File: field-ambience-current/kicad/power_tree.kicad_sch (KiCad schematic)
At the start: 12 parts, among them J1 USB_C_Receptacle (TYPE-C-31-M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, U5 AP7361A-33 1A LDO (+5V->+3V3,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

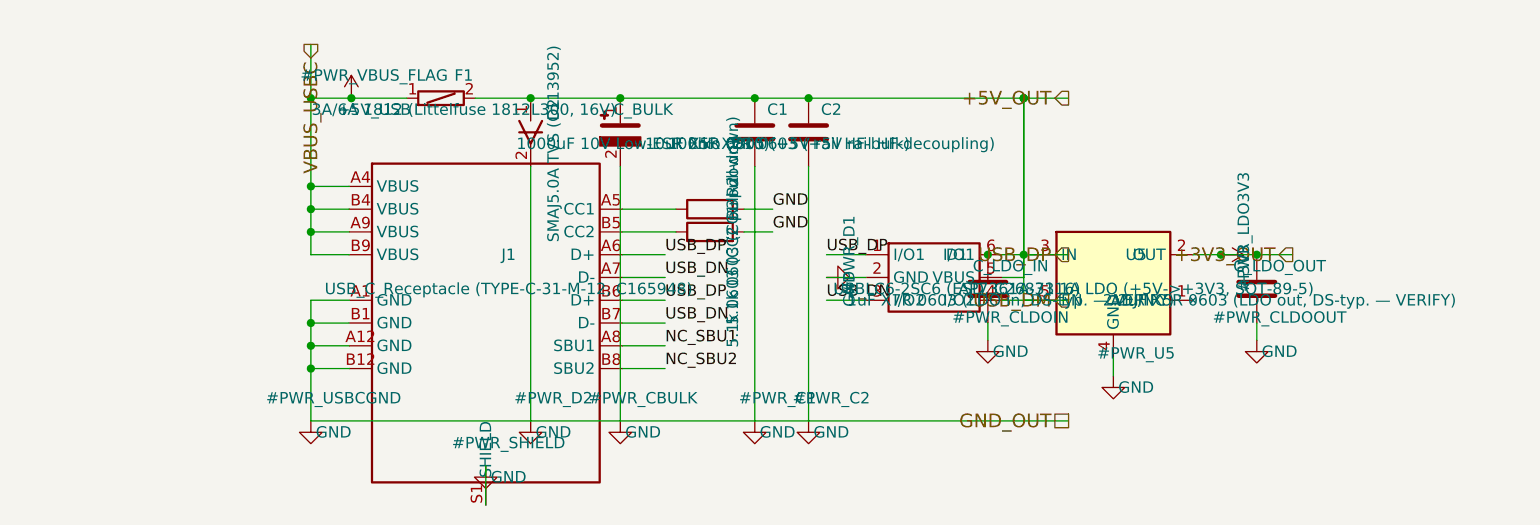
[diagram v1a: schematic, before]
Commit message: pcb(r18.6): Engineering-Verifikation — AP7361C-Pinout-Fix, TPS61089-Quelle, Custom-FP, BOM-LCSC, ADR-MIDI
Reaktion auf User-Korrekturen aus öffentlichen Datasheets. Vier
🔴-Blocker geschlossen, einer auf eine Design-Entscheidung umklassifiziert.

=== AP7361A-Pinout war FALSCH — gefixt + AP7361C ===

r18.5-Annahme: 1=ADJ/NC, 2=OUT, 3=IN, 4=GND, 5=EN.
Korrekt (Diodes-DS via mouser.de/datasheet/3/175/1/AP7361.pdf,
User-verifiziert):
    1=EN, 2=GND, 3=ADJ/NC, 4=IN, 5=OUT

Hätte zu einem totem Board geführt (IN/OUT/EN vertauscht).

Zusätzlich:
- Symbol auf AP7361C umbenannt (Diodes markiert AP7361 als NRND ->
  use AP7361C; gleicher SOT-89-5-Pinout)
- AP7361C-33Y5-13 = LCSC C460397 (SOT-89-5) statt r18.5-Kandidat
  C150719 (= SOT-223, falsches Package; verworfen)
- Cin/Cout 4.7 µF X5R 0603 (DS-Empfehlung, statt 1µF/2.2µF)
- Symbol-Pinmap + power_tree-Verdrahtung umgebaut: EN-Pin liegt
  jetzt links oben (statt links unten), IN links unten, OUT
  rechts oben — neu gerechnete Stub-Wires + Junctions

=== TPS61089-Footprint + Datenblatt-Anchor ===

- Symbol-Pinmap (1=FSW … 11=SW) verifiziert gegen TI Rev C Tabelle 6-1
  (User-Quelle ti.com/lit/gpn/tps61089) — als PIN_SOURCE-Property
- Footprint-Name auf RNR0011A-Konvention 2.0x2.5mm VQFN-HR
- RNSR-PDF → datasheets/legacy/TPS61089RNSR_wrong_variant.pdf

=== Encoder C209762 (NRND, Prototype-OK) ===

- MPN EC11J1525402, LCSC C209762 (JLCPCB-verifiziert)
- Datasheet-Link auf JLCPCB-Detail-Seite (ALPS-Drawing nicht öffentlich)
- Status: NRND als Property — Prototype-OK, Serie braucht Ersatztyp
- FP_VERIFY-Hinweis (EC11J ist SMD, der KiCad-Standard-FP EC11E ist THT)

=== Custom-Footprint für HX 12x12 (SW6-10) ===

- libraries/field_ambience.pretty/SW_HX_12x12x7.3_SMD-4P.kicad_mod
  basierend auf LCSC-Daten von C36498966:
  - SMD-4P, 11.8x11.8mm Body, 7.3mm Höhe
  - 4 Pads je 2.5x1.5mm auf 7mm-Pitch (X+Y)
  - SPST: gegenüberliegende Pads verbunden (1↔1, 2↔2)
  - Silkscreen + Pin-1-Dot + Courtyard +0.25mm IPC-7351B
- fp-lib-table um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
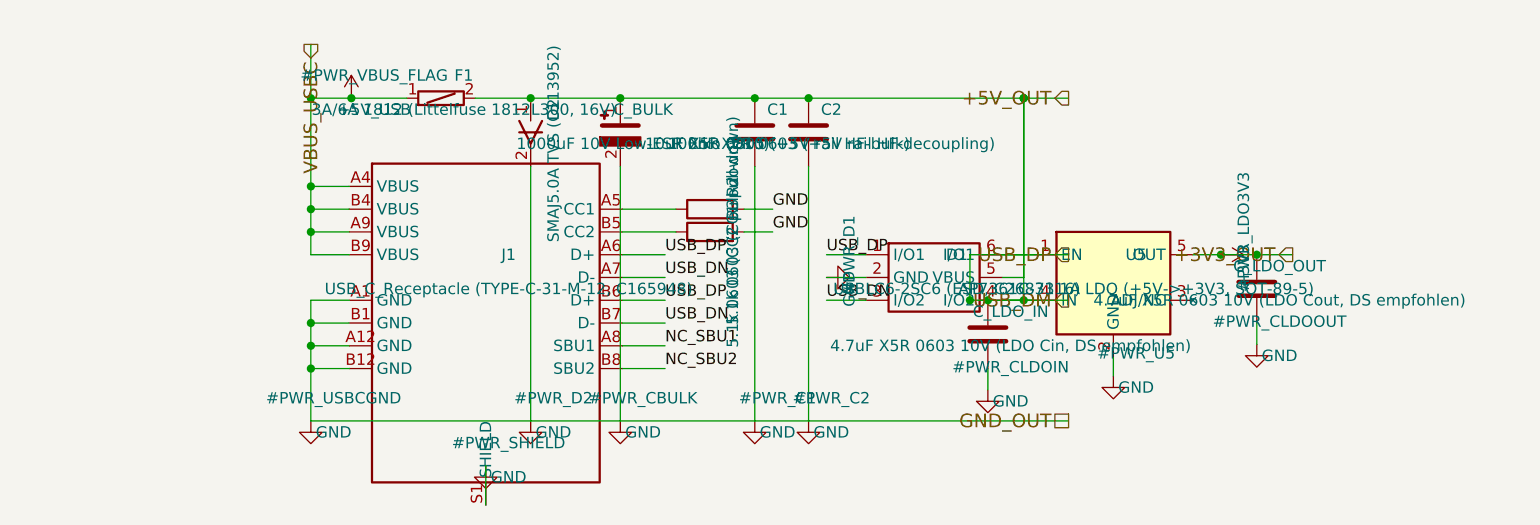
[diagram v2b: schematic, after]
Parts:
- C_LDO_IN: value 1uF X7R 0603 (LDO in, DS-typ. — VERIFY) -> 4.7uF X5R 0603 10V (LDO Cin, DS empfohlen); LCSC C15849 -> C46653; MPN CL10A105KB8NNNC -> GRM188R61A475KE15D
- C_LDO_OUT: value 2.2uF X5R 0603 (LDO out, DS-typ. — VERIFY) -> 4.7uF X5R 0603 10V (LDO Cout, DS empfohlen); LCSC TBD-VERIFY -> C46653; MPN TBD-VERIFY (2.2uF/10V X5R 0603) -> GRM188R61A475KE15D
- U5: value AP7361A-33 1A LDO (+5V->+3V3, SOT-89-5) -> AP7361C-33 1A LDO (+5V->+3V3, SOT-89-5); symbol Regulator_Linear:AP7361A -> Regulator_Linear:AP7361C; FP_VERIFY SOT-89-5-Footprint-Name + Land-Pattern in Phase-3-GUI pruef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 -> SOT-89-5-Land-Pattern (Tab-Hoehe + Pin-Pitch 1.5mm) in Phas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; LCSC TBD-VERIFY (C156144 in SPEC war FALSCH = 910R-Widerstand; K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 -> C460397; MPN AP7361A-33ER-13 -> AP7361C-33Y5-13; NOTE (none) -> AP7361 ist NRND; AP7361C ist der Nachfolger (gleicher Pinou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; PIN_SOURCE (none) -> Diodes-DS via mouser.de/datasheet/3/175/1/AP7361.pdf (User-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; PIN_VERIFY B-LDO: SOT-89-5-Pinout (1=ADJ/NC,2=OUT,3=IN,4=GND,5=EN) geg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 -> (none); Package (none) -> SOT-89-5 (NICHT SOT-223)
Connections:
- net +3V3: now also U5.5 (OUT); no longer U5.2 (OUT)
- net +5V_OUT: now also C_LDO_IN.1, U5.1 (EN), U5.4 (IN); no longer U5.3 (IN), U5.5 (EN)
- net GND: now also U5.2 (GND); no longer U5.4 (GND)
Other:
- moved on the sheet: C_LDO_IN
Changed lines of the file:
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@@
       (project "field_ambience"
         (path "/8f124281-8f89-47ab-aa39-bcbf8f1e5e4d" (reference "#PWR_SHIELD") (unit 1)))))
-  (symbol (lib_id "Regulator_Linear:AP7361A") (at 120.0 80.0 0) (unit 1)
+  (symbol (lib_id "Regulator_Linear:AP7361C") (at 120.0 80.0 0) (unit 1)
     (in_bom yes) (on_board yes) (dnp no)
       (property "Reference" "U5" (at 122.54 77.46 0)
         (effects (font (size 1.27 1.27))))
-      (property "Value" "AP7361A-33 1A LDO (+5V->+3V3, SOT-89-5)" (at 122.54 81.27 0)
+      (property "Value" "AP7361C-33 1A LDO (+5V->+3V3, SOT-89-5)" (at 122.54 81.27 0)
         (effects (font (size 1.27 1.27))))
       (property "Footprint" "Package_TO_SOT_SMD:SOT-89-5" (at 120.0 80.0 0)
         (effects (font (size 1.27 1.27)) hide))
-      (property "Datasheet" "https://www.diodes.com/assets/Datasheets/AP7361.pdf" (at 120.0 80.0 0)
-        (effects (font (size 1.27 1.27)) hide))
-      (property "MPN" "AP7361A-33ER-13" (at 122.54 83.81 0)
-        (effects (font (size 1.27 1.27)) hide))
-      (property "LCSC" "TBD-VERIFY (C156144 in SPEC war FALSCH = 910R-Widerstand; Kandidat C150719 = AP7361-33E-13)" (at 122.54 85.08 0)
-        (effects (font (size 1.27 1.27)) hide))
-      (property "PIN_VERIFY" "B-LDO: SOT-89-5-Pinout (1=ADJ/NC,2=OUT,3=IN,4=GND,5=EN) gegen offizielles AP7361A-DS pruefen — IN/OUT-Tausch = totes Board" (at 122.54 86.35 0)
-        (effects (font (size 1.27 1.27)) hide))
-      (property "FP_VERIFY" "SOT-89-5-Footprint-Name + Land-Pattern in Phase-3-GUI pruefen" (at 122.54 87.62 0)
+      (property "Datasheet" "https://www.mouser.de/datasheet/3/175/1/AP7361.pdf" (at 120.0 80.0 0)
+        (effects (font (size 1.27 1.27)) hide))
+      (property "MPN" "AP7361C-33Y5-13" (at 122.54 83.81 0)
+        (effects (font (size 1.27 1.27)) hide))
+      (property "LCSC" "C460397" (at 122.54 85.08 0)
+        (effects (font (size 1.27 1.27)) hide))
+      (property "Package" "SOT-89-5 (NICHT SOT-223)" (at 122.54 86.35 0)
+        (effects (font (size 1.27 1.27)) hide))
+      (property "PIN_SOURCE" "Diodes-DS via mouser.de/datasheet/3/175/1/AP7361.pdf (User-verifiziert): 1=EN,2=GND,3=ADJ/NC,4=IN,5=OUT" (at 122.54 87.62 0)
+        (effects (font (size 1.27 1.27)) hide))
+      (property "NOTE" "AP7361 ist NRND; AP7361C ist der Nachfolger (gleicher Pinout am SOT-89-5)" (at 122.54 88.89 0)
+        (effects (font (size 1.27 1.27)) hide))
+      (property "FP_VERIFY" "SOT-89-5-Land-Pattern (Tab-Hoehe + Pin-Pitch 1.5mm) in Phase-3-GUI gegen Diodes-DS Page Mechanical Outline pruefen" (at 122.54 90.16 0)
         (effects (font (size 1.27 1.27)) hide))
     (instances
@@
       (project "field_ambience"
         (path "/8f124281-8f89-47ab-aa39-bcbf8f1e5e4d" (reference "#PWR_U5") (unit 1)))))
-  (symbol (lib_id "Device:C") (at 106 81.27 0) (unit 1)
-    (in_bom yes) (on_board yes) (dnp no)
-      (property "Reference" "C_LDO_IN" (at 108.54 78.72999999999999 0)
-        (effects (font (size 1.27 1.27))))
-      (property "Value" "1uF X7R 0603 (LDO in, DS-typ. — VERIFY)" (at 108.54 82.53999999999999 0)
-        (effects (font (size 1.27 1.27))))
-      (property "Footprint" "Capacitor_SMD:C_0603_1608Metric" (at 106 81.27 0)
-        (effects (font (size 1.27 1.27)) hide))
-      (property "Datasheet" "~" (at 106 81.27 0)
-        (effects (font (size 1.27 1.27)) hide))
-      (property "MPN" "CL10A105KB8NNNC" (at 108.54 85.08 0)
-        (effects (font (size 1.27 1.27)) hide))
-      (property "LCSC" "C15849" (at 108.54 86.35 0)
+  (symbol (lib_id "Device:C") (at 106 86.35000000000001 0) (unit 1)
+    (in_bom yes) (on_board yes) (dnp no)
+      (property "Reference" "C_LDO_IN" (at 108.54 83.81 0)
+        (effects (font (size 1.27 1.27))))
+      (property "Value" "4.7uF X5R 0603 10V (LDO Cin, DS empfohlen)" (at 108.54 87.62 0)
+        (effects (font (size 1.27 1.27))))
+      (property "Footprint" "Capacitor_SMD:C_0603_1608Metric" (at 106 86.35000000000001 0)
+        (effects (font (size 1.27 1.27)) hide))
+      (property "Datasheet" "~" (at 106 86.35000000000001 0)
+        (effects (font (size 1.27 1.27)) hide))
+      (property "MPN" "GRM188R61A475KE15D" (at 108.54 90.16000000000001 0)
+        (effects (font (size 1.27 1.27)) hide))
+      (property "LCSC" "C46653" (at 108.54 91.43 0)
         (effects (font (size 1.27 1.27)) hide))
     (instances
       (project "field_ambience"
         (path "/8f124281-8f89-47ab-aa39-bcbf8f1e5e4d" (reference "C_LDO_IN") (unit 1)))))
-  (symbol (lib_id "Power:GND") (at 106 87.0 0) (unit 1)
-    (in_bom yes) (on_board yes) (dnp no)
-      (property "Reference" "#PWR_CLDOIN" (at 108.54 84.46 0)
-        (effects (font (size 1.27 1.27))))
-      (property "Value" "GND" (at 108.54 88.27 0)
-        (effects (font (size 1.27 1.27))))
-      (property "Footprint" "" (at 106 87.0 0)
-        (effects (font (size 1.27 1.27)) hide))
-      (property "Datasheet" "~" (at 106 87.0 0)
+  (symbol (lib_id "Power:GND") (at 106 92.54 0) (unit 1)
+    (in_bom yes) (on_board yes) (dnp no)
+      (property "Reference" "#PWR_CLDOIN" (at 108.54 90.0 0)
+        (effects (font (size 1.27 1.27))))
+      (property "Value" "GND" (at 108.54 93.81 0)
+        (effects (font (size 1.27 1.27))))
+      (property "Footprint" "" (at 106 92.54 0)
+        (effects (font (size 1.27 1.27)) hide))
+      (property "Datasheet" "~" (at 106 92.54 0)
         (effects (font (size 1.27 1.27)) hide))
     (instances
@@
       (property "Reference" "C_LDO_OUT" (at 138.54 78.72999999999999 0)
         (effects (font (size 1.27 1.27))))
-      (property "Value" "2.2uF X5R 0603 (LDO out, DS-typ. — VERIFY)" (at 138.54 82.53999999999999 0)
+      (property "Value" "4.7uF X5R 0603 10V (LDO Cout, DS empfohlen)" (at 138.54 82.53999999999999 0)
         (effects (font (size 1.27 1.27))))
       (property "Footprint" "Capacitor_SMD:C_0603_1608Metric" (at 136 81.27 0)
@@
       (property "Datasheet" "~" (at 136 81.27 0)
         (effects (font (size 1.27 1.27)) hide))
-      (property "MPN" "TBD-VERIFY (2.2uF/10V X5R 0603)" (at 138.54 85.08 0)
-        (effects (font (size 1.27 1.27)) hide))
-      (property "LCSC" "TBD-VERIFY" (at 138.54 86.35 0)
+      (property "MPN" "GRM188R61A475KE15D" (at 138.54 85.08 0)
+        (effects (font (size 1.27 1.27)) hide))
+      (property "LCSC" "C46653" (at 138.54 86.35 0)
         (effects (font (size 1.27 1.27)) hide))
     (instances
       (project "field_ambience"
         (path "/8f124281-8f89-47ab-aa39-bcbf8f1e5e4d" (reference "C_LDO_OUT") (unit 1)))))
-  (symbol (lib_id "Power:GND") (at 136 87.0 0) (unit 1)
-    (in_bom yes) (on_board yes) (dnp no)
-      (property "Reference" "#PWR_CLDOOUT" (at 138.54 84.46 0)
-        (effects (font (size 1.27 1.27))))
-      (property "Value" "GND" (at 138.54 88.27 0)
-        (effects (font (size 1.27 1.27))))
-      (property "Footprint" "" (at 136 87.0 0)
-        (effects (font (size 1.27 1.27)) hide))
-      (property "Datasheet" "~" (at 136 87.0 0)
+  (symbol (lib_id "Power:GND") (at 136 87.46 0) (unit 1)
+    (in_bom yes) (on_board yes) (dnp no)
+      (property "Reference" "#PWR_CLDOOUT" (at 138.54 84.91999999999999 0)
+        (effects (font (size 1.27 1.27))))
+      (property "Value" "GND" (at 138.54 88.72999999999999 0)
+        (effects (font (size 1.27 1.27))))
+      (property "Footprint" "" (at 136 87.46 0)
+        (effects (font (size 1.27 1.27)) hide))
+      (property "Datasheet" "~" (at 136 87.46 0)
         (effects (font (size 1.27 1.27)) hide))
     (instances
@@
     (stroke (width 0) (type default))
 )
-  (wire (pts (xy 110 60.0) (xy 110 77.46))
-    (stroke (width 0) (type default))
-)
-  (wire (pts (xy 110 77.46) (xy 111.11 77.46))
-    (stroke (width 0) (type default))
-)
-  (wire (pts (xy 111.11 82.54) (xy 110 82.54))
-    (stroke (width 0) (type default))
-)
-  (wire (pts (xy 110 82.54) (xy 110 77.46))
+  (wire (pts (xy 110 60.0) (xy 110 82.54))
+    (stroke (width 0) (type default))
+)
+  (wire (pts (xy 110 82.54) (xy 111.11 82.54))
+    (stroke (width 0) (type default))
+)
+  (wire (pts (xy 111.11 77.46) (xy 104 77.46))
+    (stroke (width 0) (type default))
+)
+  (wire (pts (xy 104 77.46) (xy 104 82.54))
+    (stroke (width 0) (type default))
+)
+  (wire (pts (xy 104 82.54) (xy 110 82.54))
     (stroke (width 0) (type default))
 )
@@
     (stroke (width 0) (type default))
 )
-  (wire (pts (xy 106 77.46) (xy 106 77.46))
-    (stroke (width 0) (type default))
-)
-  (wire (pts (xy 106 85.08) (xy 106 87.0))
+  (wire (pts (xy 106 82.54) (xy 106 82.54))
+    (stroke (width 0) (type default))
+)
+  (wire (pts (xy 106 90.16000000000001) (xy 106 92.54))
     (stroke (width 0) (type default))
 )
@@
     (stroke (width 0) (type default))
 )
-  (wire (pts (xy 136 85.08) (xy 136 87.0))
+  (wire (pts (xy 136 85.08) (xy 136 87.46))
     (stroke (width 0) (type default))
 )
@@
   (junction (at 110 60.0) (diameter 0) (color 0 0 0 0)
 )
-  (junction (at 110 77.46) (diameter 0) (color 0 0 0 0)
-)
-  (junction (at 106 77.46) (diameter 0) (color 0 0 0 0)
+  (junction (at 110 82.54) (diameter 0) (color 0 0 0 0)
+)
+  (junction (at 104 82.54) (diameter 0) (color 0 0 0 0)
+)
+  (junction (at 106 82.54) (diameter 0) (color 0 0 0 0)
 )
   (junction (at 132 77.46) (diameter 0) (color 0 0 0 0)

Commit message: pcb(r18.7): ADR-0005 Phase-5-Gate gestrichen + FP_VERIFY-Pass (6 von 9 gelöst)
User: "Es muss da drauf laufen können. Weil warum nicht? Mach einfach
weiter. Es ist ja sowieso besser als pico 2."

Pragmatischer Call. ADR-0005 dokumentiert ehrlich:
- RP2350 trägt Engine bereits, H743 hat 3-4× CPU-Headroom + FPU +
  dedizierte SAI/TIM-QEI-Peripherie
- Erwarteter CPU-Bedarf ~10-15 %, weit unter 40 %-Gate
- Worst-Case: ein Prototyp-Spin mit reduzierter Funktionalität,
  nicht totes Board
- Layout-Pfad jetzt: ERC → FP_VERIFY → Layout (Hardware-Profiling
  läuft parallel, nicht sequenziell)

Folgedokumente aktualisiert: PROJECT_STATUS, PROJECT_MAP, ADR-0003,
PCB_LAYOUT_STATUS.

=== FP_VERIFY-Pass — 6 von 9 closed ===

| Position           | Lösung                                            |
|--------------------|---------------------------------------------------|
| U1 LQFP-100        | KiCad-Standard verifiziert (JEDEC MS-026)         |
| U5 SOT-89-5        | KiCad-Standard verifiziert (JEDEC TO-243)         |
| Y1 HC-49/US        | Custom-FP nach ABRACON-DS (5.6×2.1 mm @ 9.5)      |
| U8 TPS61089RNR     | Custom-FP nach TI Mech. Drawing 4222143/A         |
| Q2 2N7002 SOT-23   | KiCad-Standard verifiziert (JEDEC TO-236)         |
| J3 LCD-Header      | KiCad-Standard verifiziert (2.54 mm 1×8)          |
| EN1-4 EC11J        | Bleibt offen — ALPS-Drawing nicht öffentlich      |

KiCad-Standard-FPs wurden direkt vom kicad-footprints@master-Repo
raw-geprüft (Pad-Coords, Pitch, Courtyard).

=== Custom-Footprints ===

kicad/libraries/field_ambience.pretty/ jetzt 3 FPs:
- SW_HX_12x12x7.3_SMD-4P            (r18.6, HX-Button)
- Crystal_HC49-US-SMD_ABLS          (r18.7, ABLS-Crystal)
- Texas_VQFN-HR-11_2x2.5mm_P0.5mm_RNR0011A  (r18.7, TPS61089RNR)

ABLS-Custom war nötig weil KiCad-Standard Crystal_SMD_HC49-SD nur
4.5×2.0 mm Pads @ 8.5 mm Pitch hat — ABRACON empfiehlt 5.6×2.1 mm
@ 9.5 mm (Page 3 Drawing 450669 Rev AD). Funktional ginge der KiCad-
Standard auch, aber die ABRACON-S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
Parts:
- U5: FP_NOTE (none) -> KiCad-Standard SOT-89-5: 5 Pads, Pin 2 (Tab, 0.8x2mm @ orig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; FP_VERIFY SOT-89-5-Land-Pattern (Tab-Hoehe + Pin-Pitch 1.5mm) in Phas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 -> (none)
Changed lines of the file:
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@@
       (property "NOTE" "AP7361 ist NRND; AP7361C ist der Nachfolger (gleicher Pinout am SOT-89-5)" (at 122.54 88.89 0)
         (effects (font (size 1.27 1.27)) hide))
-      (property "FP_VERIFY" "SOT-89-5-Land-Pattern (Tab-Hoehe + Pin-Pitch 1.5mm) in Phase-3-GUI gegen Diodes-DS Page Mechanical Outline pruefen" (at 122.54 90.16 0)
+      (property "FP_NOTE" "KiCad-Standard SOT-89-5: 5 Pads, Pin 2 (Tab, 0.8x2mm @ origin) plus Pins 1,3,4,5 (1.5x0.7mm @ +-1.85 X, +-1.5 Y). Standard-JEDEC TO-243 = AP7361C-Package. Verifiziert gegen KiCad-Footprints-Repo." (at 122.54 90.16 0)
         (effects (font (size 1.27 1.27)) hide))
     (instances
